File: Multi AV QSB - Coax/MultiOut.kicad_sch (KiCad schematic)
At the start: 7 parts, among them J1 Multi AV, J2 R, J3 G, J4 B

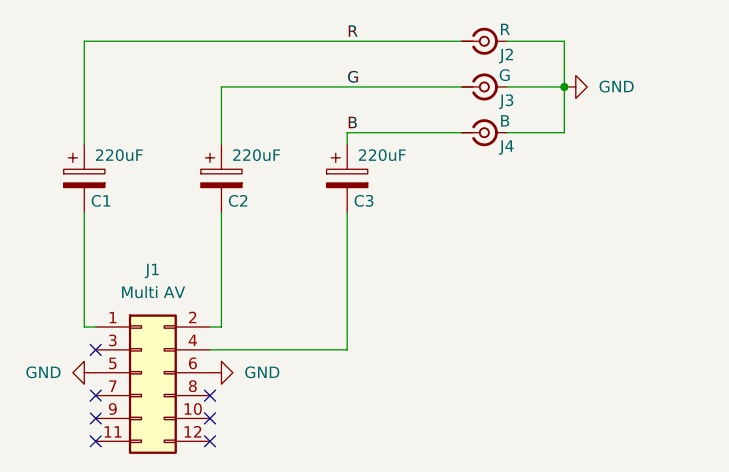
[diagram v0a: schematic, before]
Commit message: QSB - remove AC coupling and add GND lift jumper
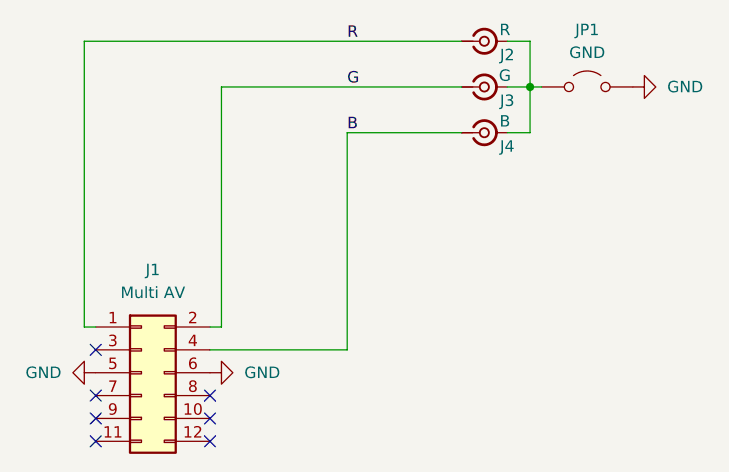
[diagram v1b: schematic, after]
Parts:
- removed C1, C2, C3: 220uF, Capacitor_SMD:CP_Elec_5x5.8, symbol Device:C_Polarized
- added JP1: GND, Jumper:SolderJumper-2_P1.3mm_Open_RoundedPad1.0x1.5mm, symbol Jumper:Jumper_2_Open
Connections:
- net B: now also J1.4 (Pin_4)
- net G: now also J1.2 (Pin_2)
- net GND: now also JP1.2 (B); no longer J2.2 (Ext), J3.2 (Ext), J4.2 (Ext)
- net R: now also J1.1 (Pin_1)
- new net: J2.2 (Ext), J3.2 (Ext), J4.2 (Ext), JP1.1 (A)
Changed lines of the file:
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@@
 	)
 	(junction
-		(at 190.5 55.88)
+		(at 186.69 55.88)
 		(diameter 0)
 		(color 0 0 0 0)
@@
 	(wire
 		(pts
+			(xy 186.69 55.88) (xy 187.96 55.88)
+		)
+		(stroke
+			(width 0)
+			(type default)
+		)
+	)
+	(wire
+		(pts
 			(xy 137.16 50.8) (xy 179.07 50.8)
 		)
@@
 	(wire
 		(pts
-			(xy 184.15 50.8) (xy 190.5 50.8)
-		)
-		(stroke
-			(width 0)
-			(type default)
-		)
-	)
-	(wire
-		(pts
-			(xy 184.15 60.96) (xy 190.5 60.96)
-		)
-		(stroke
-			(width 0)
-			(type default)
-		)
-	)
-	(wire
-		(pts
-			(xy 184.15 55.88) (xy 190.5 55.88)
-		)
-		(stroke
-			(width 0)
-			(type default)
-		)
-	)
-	(wire
-		(pts
-			(xy 137.16 62.23) (xy 137.16 50.8)
-		)
-		(stroke
-			(width 0)
-			(type default)
-		)
-	)
-	(wire
-		(pts
-			(xy 137.16 69.85) (xy 137.16 82.55)
+			(xy 186.69 50.8) (xy 186.69 55.88)
+		)
+		(stroke
+			(width 0)
+			(type default)
+		)
+	)
+	(wire
+		(pts
+			(xy 137.16 50.8) (xy 137.16 82.55)
+		)
+		(stroke
+			(width 0)
+			(type default)
+		)
+	)
+	(wire
+		(pts
+			(xy 184.15 50.8) (xy 186.69 50.8)
 		)
 		(stroke
@@
 	(wire
 		(pts
+			(xy 184.15 60.96) (xy 186.69 60.96)
+		)
+		(stroke
+			(width 0)
+			(type default)
+		)
+	)
+	(wire
+		(pts
 			(xy 152.4 55.88) (xy 179.07 55.88)
 		)
@@
 	(wire
 		(pts
-			(xy 190.5 50.8) (xy 190.5 55.88)
-		)
-		(stroke
-			(width 0)
-			(type default)
-		)
-	)
-	(wire
-		(pts
-			(xy 166.37 69.85) (xy 166.37 85.09)
-		)
-		(stroke
-			(width 0)
-			(type default)
-		)
-	)
-	(wire
-		(pts
 			(xy 137.16 82.55) (xy 138.43 82.55)
 		)
@@
 	(wire
 		(pts
-			(xy 190.5 60.96) (xy 190.5 55.88)
-		)
-		(stroke
-			(width 0)
-			(type default)
-		)
-	)
-	(wire
-		(pts
-			(xy 152.4 69.85) (xy 152.4 82.55)
-		)
-		(stroke
-			(width 0)
-			(type default)
-		)
-	)
-	(wire
-		(pts
-			(xy 166.37 60.96) (xy 166.37 62.23)
-		)
-		(stroke
-			(width 0)
-			(type default)
-		)
-	)
-	(wire
-		(pts
-			(xy 152.4 55.88) (xy 152.4 62.23)
+			(xy 184.15 55.88) (xy 186.69 55.88)
+		)
+		(stroke
+			(width 0)
+			(type default)
+		)
+	)
+	(wire
+		(pts
+			(xy 166.37 60.96) (xy 166.37 85.09)
+		)
+		(stroke
+			(width 0)
+			(type default)
+		)
+	)
+	(wire
+		(pts
+			(xy 186.69 60.96) (xy 186.69 55.88)
+		)
+		(stroke
+			(width 0)
+			(type default)
+		)
+	)
+	(wire
+		(pts
+			(xy 152.4 55.88) (xy 152.4 82.55)
 		)
 		(stroke
@@
 	)
 	(symbol
-		(lib_id "Device:C_Polarized")
-		(at 137.16 66.04 0)
+		(lib_id "Jumper:Jumper_2_Open")
+		(at 193.04 55.88 0)
 		(unit 1)
 		(exclude_from_sim no)
@@
 		(on_board yes)
 		(dnp no)
-		(property "Reference" "C1"
-			(at 140.208 68.58 0)
-			(effects
-				(font
-					(size 1.27 1.27)
-				)
-				(justify right)
-			)
-		)
-		(property "Value" "220uF"
-			(at 143.764 63.5 0)
-			(effects
-				(font
-					(size 1.27 1.27)
-				)
-				(justify right)
-			)
-		)
-		(property "Footprint" "Capacitor_SMD:CP_Elec_5x5.8"
-			(at 138.1252 69.85 0)
+		(fields_autoplaced yes)
+		(property "Reference" "JP1"
+			(at 193.04 49.53 0)
+			(effects
+				(font
+					(size 1.27 1.27)
+				)
+			)
+		)
+		(property "Value" "GND"
+			(at 193.04 52.07 0)
+			(effects
+				(font
+					(size 1.27 1.27)
+				)
+			)
+		)
+		(property "Footprint" "Jumper:SolderJumper-2_P1.3mm_Open_RoundedPad1.0x1.5mm"
+			(at 193.04 55.88 0)
 			(effects
 				(font
@@
 		)
 		(property "Datasheet" "~"
-			(at 137.16 66.04 0)
-			(effects
-				(font
-					(size 1.27 1.27)
-				)
-				(hide yes)
-			)
-		)
-		(property "Description" "Polarized capacitor"
-			(at 137.16 66.04 0)
-			(effects
-				(font
-					(size 1.27 1.27)
-				)
-				(hide yes)
-			)
+			(at 193.04 55.88 0)
+			(effects
+				(font
+					(size 1.27 1.27)
+				)
+				(hide yes)
+			)
+		)
+		(property "Description" "Jumper, 2-pole, open"
+			(at 193.04 55.88 0)
+			(effects
+				(font
+					(size 1.27 1.27)
+				)
+				(hide yes)
+			)
+		)
+		(pin "2"
 		)
 		(pin "1"
-		)
-		(pin "2"
 		)
 		(instances
 			(project ""
 				(path "/be8cd0e2-c518-4bbf-a245-612707f908c9"
-					(reference "C1")
+					(reference "JP1")
 					(unit 1)
 				)
@@
 	)
 	(symbol
-		(lib_id "Device:C_Polarized")
-		(at 166.37 66.04 0)
-		(unit 1)
-		(exclude_from_sim no)
-		(in_bom yes)
-		(on_board yes)
-		(dnp no)
-		(property "Reference" "C3"
-			(at 169.418 68.58 0)
-			(effects
-				(font
-					(size 1.27 1.27)
-				)
-				(justify right)
-			)
-		)
-		(property "Value" "220uF"
-			(at 172.974 63.5 0)
-			(effects
-				(font
-					(size 1.27 1.27)
-				)
-				(justify right)
-			)
-		)
-		(property "Footprint" "Capacitor_SMD:CP_Elec_5x5.8"
-			(at 167.3352 69.85 0)
-			(effects
-				(font
-					(size 1.27 1.27)
-				)
-				(hide yes)
-			)
-		)
-		(property "Datasheet" "~"
-			(at 166.37 66.04 0)
-			(effects
-				(font
-					(size 1.27 1.27)
-				)
-				(hide yes)
-			)
-		)
-		(property "Description" "Polarized capacitor"
-			(at 166.37 66.04 0)
-			(effects
-				(font
-					(size 1.27 1.27)
-				)
-				(hide yes)
-			)
-		)
-		(pin "1"
-		)
-		(pin "2"
-		)
-		(instances
-			(project "MultiOut"
-				(path "/be8cd0e2-c518-4bbf-a245-612707f908c9"
-					(reference "C3")
-					(unit 1)
-				)
-			)
-		)
-	)
-	(symbol
 		(lib_id "power:GND")
-		(at 190.5 55.88 90)
+		(at 198.12 55.88 90)
 		(unit 1)
 		(exclude_from_sim no)
@@
 		(fields_autoplaced yes)
 		(property "Reference" "#PWR01"
-			(at 196.85 55.88 0)
+			(at 204.47 55.88 0)
 			(effects
 				(font
@@
 		)
 		(property "Value" "GND"
-			(at 194.31 55.8799 90)
+			(at 201.93 55.8799 90)
 			(effects
 				(font
@@
 		)
 		(property "Footprint" ""
-			(at 190.5 55.88 0)
+			(at 198.12 55.88 0)
 			(effects
 				(font
@@
 		)
 		(property "Datasheet" ""
-			(at 190.5 55.88 0)
+			(at 198.12 55.88 0)
 			(effects
 				(font
@@
 		)
 		(property "Description" "Power symbol creates a global label with name \"GND\" , ground"
-			(at 190.5 55.88 0)
+			(at 198.12 55.88 0)
 			(effects
 				(font
@@
 					(unit 1)
 				)
-			)
-		)
-	)
-	(symbol
-		(lib_id "Device:C_Polarized")
-		(at 152.4 66.04 0)
-		(unit 1)
-		(exclude_from_sim no)
-		(in_bom yes)
-		(on_board yes)
-		(dnp no)
-		(property "Reference" "C2"
-			(at 155.448 68.58 0)
-			(effects
-				(font
-					(size 1.27 1.27)
-				)
-				(justify right)
-			)
-		)
-		(property "Value" "220uF"
-			(at 159.004 63.5 0)
-			(effects
-				(font
-					(size 1.27 1.27)
-				)
-				(justify right)
-			)
-		)
-		(property "Footprint" "Capacitor_SMD:CP_Elec_5x5.8"
-			(at 153.3652 69.85 0)
-			(effects
-				(font
-					(size 1.27 1.27)
-				)
-				(hide yes)
-			)
-		)
-		(property "Datasheet" "~"
-			(at 152.4 66.04 0)
-			(effects
-				(font
-					(size 1.27 1.27)
-				)
-				(hide yes)
-			)
-		)
-		(property "Description" "Polarized capacitor"
-			(at 152.4 66.04 0)
-			(effects
-				(font
-					(size 1.27 1.27)
-				)
-				(hide yes)
-			)
-		)
-		(pin "1"
-		)
-		(pin "2"
-		)
-		(instances
-			(project "MultiOut"
-				(path "/be8cd0e2-c518-4bbf-a245-612707f908c9"
-					(reference "C2")
-					(unit 1)
-				)
